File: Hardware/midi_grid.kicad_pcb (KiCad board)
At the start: 2 copper layers, 275 x 200 mm, 329 parts, among them J1 USB_OTG, J2 3.5mm jack, J3 3.5mm jack, J4 Conn_01x04_Male, M1 Mounting_hole, M2 Mounting_hole, M3 Mounting_hole, Q1 BSS83P, Q10 BSS83P, Q11 BSS83P, Q12 BSS83P, Q13 BSS83P, Q14 BSS83P, Q15 BSS83P, Q16 BSS83P, Q17 BSS83P, Q18 BSS83P, Q19 BSS83P, Q2 BSS83P, Q20 BSS83P, Q21 NX7002AK, Q22 NX7002AK, Q23 NX7002AK, Q24 NX7002AK, Q25 NX7002AK, Q26 NX7002AK, Q27 NX7002AK, Q28 NX7002AK, Q29 NX7002AK, Q3 BSS83P, Q30 NX7002AK, Q31 NX7002AK, Q32 NX7002AK, Q33 NX7002AK, Q34 NX7002AK, Q4 BSS83P, Q5 BSS83P, Q6 BSS83P, Q7 BSS83P, Q8 BSS83P, Q9 BSS83P, SW1 Button_matrix_4x4, SW10 SW_Push, SW11 SW_Push, SW12 SW_Push, SW13 SW_Push, SW14 SW_Push, SW15 SW_Push, SW16 SW_Push, SW17 SW_Push, SW18 SW_Push, SW19 SW_Push, SW2 Button_matrix_4x4, SW20 SW_Push, SW21 SW_Push, SW22 SW_Push, SW23 SW_Push, SW24 SW_Push, SW25 EC12E24204A9, SW26 EC12E24204A9, SW3 Button_matrix_4x4, SW4 Button_matrix_4x4, SW5 SW_Push, SW6 SW_Push, SW7 SW_Push, SW8 SW_Push, SW9 SW_Push, U1 STM32F411RCT6, U2 74HC138, U3 74HC138, U4 74HC138, U5 USBUF, U6 LTV-357T, U7 LD1117STR, Y1 8MHz

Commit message: added BOM, changed names of some components in the schematic
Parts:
- Q1, Q10, Q11, Q12, Q13, Q14, Q15, Q16, Q17, Q18, Q19, Q2, Q20, Q3, Q4, Q5, Q6, Q7, Q8, Q9: value BSS83P -> BSH205G2
- R21, R22, R23, R24: value 10K -> 1K
- R25, R26, R27, R28, R33, R34, R35, R36, R41, R42, R43, R44: value 100 -> 100R
- R57, R58, R60, R61, R62: value 220 -> 220R
- U2, U3, U4: value 74HC138 -> SN74HC138PW
- U5: value USBUF -> USBUF02W6
- U6: value LTV-357T -> VO617A

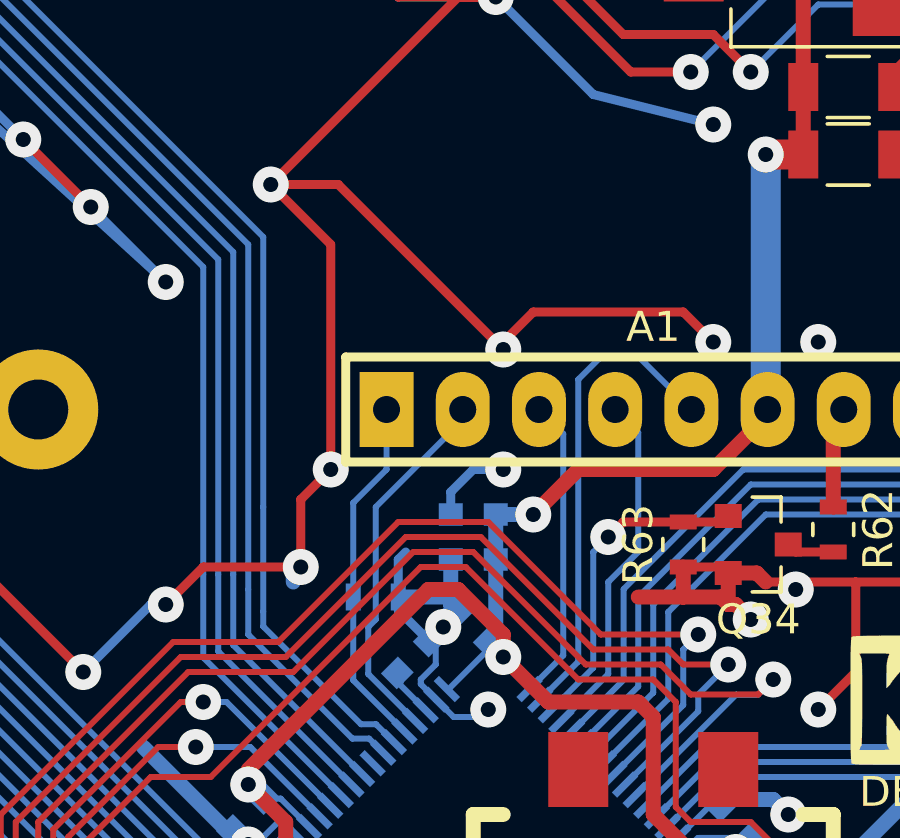
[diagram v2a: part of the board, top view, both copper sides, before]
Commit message: changed pin of LCD CS, so hardware chip select could be used
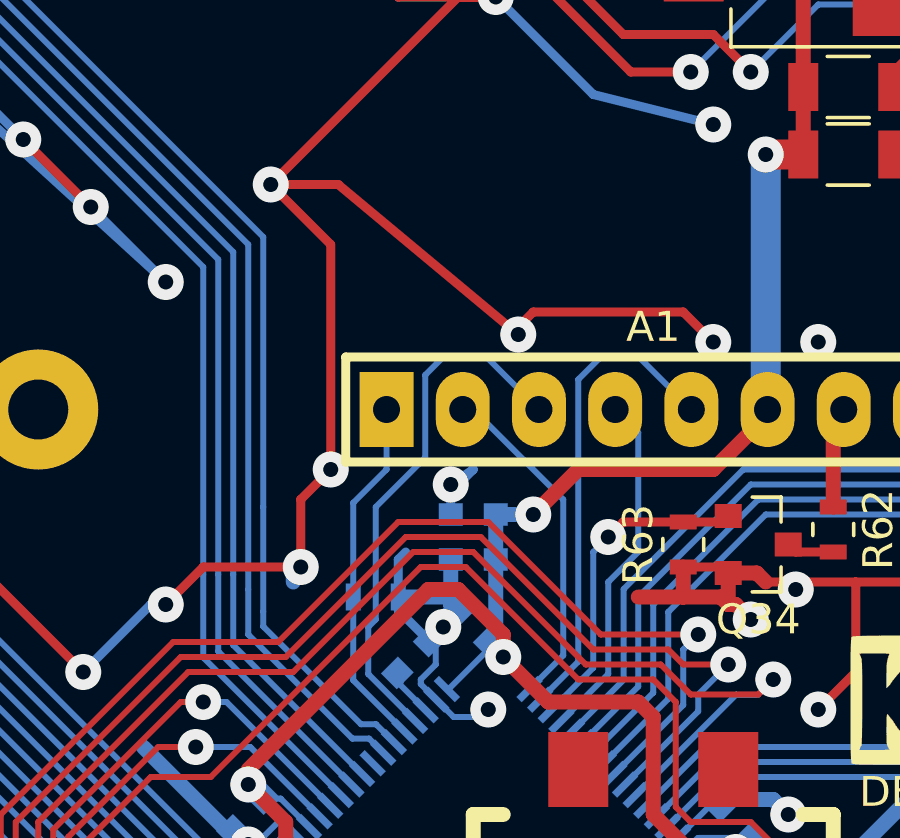
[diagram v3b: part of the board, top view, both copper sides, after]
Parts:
- U2, U3, U4: value SN74HC138PW -> 74HC138
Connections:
- U1 pad 29: /digital_io/LCD_CS -> /digital_io/LCD_DC
- U1 pad 33: /digital_io/LCD_DC -> /digital_io/LCD_CS
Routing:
- net /digital_io/LCD_DC: track 10.1 -> 17.7 mm
- net /digital_io/LCD_CS: track 12.3 -> 11.4 mm
- net GND: track 3946.7 -> 3945.9 mm
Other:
- board text added: "Designed by Gediminas Žukaitis Version 1.1 github.com/zukaitis/midi-grid Date of revision: 2018-01-27"
- board text removed: "Designed by Gediminas Žukaitis Version 1.0 github.com/zukaitis/midi-grid Date of revision: 2018-01-20"
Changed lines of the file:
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@@
     (thickness 1.6)
     (drawings 17)
-    (tracks 4692)
+    (tracks 4697)
     (zones 0)
     (modules 329)
@@
   )
   (setup
-    (last_trace_width 0.5)
+    (last_trace_width 0.2)
     (user_trace_width 0.2)
     (user_trace_width 0.3)
@@
       (effects (font (size 1 1) (thickness 0.15)) (justify mirror))
     )
-    (fp_text value SN74HC138PW (at 0 -3.55) (layer B.Fab)
+    (fp_text value 74HC138 (at 0 -3.55) (layer B.Fab)
       (effects (font (size 1 1) (thickness 0.15)) (justify mirror))
     )
@@
       (effects (font (size 1 1) (thickness 0.15)) (justify mirror))
     )
-    (fp_text value SN74HC138PW (at 0 -3.55 180) (layer B.Fab)
+    (fp_text value 74HC138 (at 0 -3.55 180) (layer B.Fab)
       (effects (font (size 1 1) (thickness 0.15)) (justify mirror))
     )
@@
       (effects (font (size 1 1) (thickness 0.15)) (justify mirror))
     )
-    (fp_text value SN74HC138PW (at 0 -3.55 180) (layer B.Fab)
+    (fp_text value 74HC138 (at 0 -3.55 180) (layer B.Fab)
       (effects (font (size 1 1) (thickness 0.15)) (justify mirror))
     )
@@
       (net 143 /digital_io/LCD_RESET))
     (pad 29 smd rect (at 2.25 -5.7 315) (size 1 0.25) (layers B.Cu B.Paste B.Mask)
-      (net 140 /digital_io/LCD_CS))
+      (net 166 /digital_io/LCD_DC))
     (pad 30 smd rect (at 2.75 -5.7 315) (size 1 0.25) (layers B.Cu B.Paste B.Mask)
       (net 165 /mcu/VCAP))
@@
       (net 2 +3V3))
     (pad 33 smd rect (at 5.7 -3.75 45) (size 1 0.25) (layers B.Cu B.Paste B.Mask)
-      (net 166 /digital_io/LCD_DC))
+      (net 140 /digital_io/LCD_CS))
     (pad 34 smd rect (at 5.7 -3.25 45) (size 1 0.25) (layers B.Cu B.Paste B.Mask)
       (net 141 /digital_io/LCD_SCLK))
@@
     (effects (font (size 1 1) (thickness 0.2)))
   )
-  (gr_text "Designed by Gediminas Žukaitis\nVersion 1.0\ngithub.com/zukaitis/midi-grid\nDate of revision: 2018-01-20" (at 225.5 214.25) (layer B.SilkS)
+  (gr_text "Designed by Gediminas Žukaitis\nVersion 1.1\ngithub.com/zukaitis/midi-grid\nDate of revision: 2018-01-27" (at 225.5 214.25) (layer B.SilkS)
     (effects (font (size 2 2) (thickness 0.4)) (justify left mirror))
   )
@@
   (via (at 268 117.75) (size 1.2) (drill 0.5) (layers F.Cu B.Cu) (net 1))
   (segment (start 268.45 117.3) (end 268 117.75) (width 0.3) (layer B.Cu) (net 1))
-  (segment (start 310.5 78.5) (end 310.5 78.25) (width 0.3) (layer F.Cu) (net 1))
+  (segment (start 311 78) (end 311 77.75) (width 0.3) (layer F.Cu) (net 1))
   (via (at 317.5 78.25) (size 1.2) (drill 0.5) (layers F.Cu B.Cu) (net 1))
   (segment (start 317.5 78) (end 317.5 78.25) (width 0.3) (layer B.Cu) (net 1))
-  (segment (start 305 73) (end 310.5 78.5) (width 0.3) (layer F.Cu) (net 1))
+  (segment (start 305 73) (end 311 78) (width 0.3) (layer F.Cu) (net 1))
   (via (at 302.75 73) (size 1.2) (drill 0.5) (layers F.Cu B.Cu) (net 1))
-  (via (at 310.5 78.5) (size 1.2) (drill 0.5) (layers F.Cu B.Cu) (net 1))
+  (via (at 311 78) (size 1.2) (drill 0.5) (layers F.Cu B.Cu) (net 1))
   (segment (start 305 73) (end 302.75 73) (width 0.3) (layer F.Cu) (net 1))
   (segment (start 316.5 77.25) (end 317.5 78.25) (width 0.3) (layer F.Cu) (net 1))
   (segment (start 311.5 77.25) (end 316.5 77.25) (width 0.3) (layer F.Cu) (net 1))
-  (segment (start 310.5 78.25) (end 311.5 77.25) (width 0.3) (layer F.Cu) (net 1))
+  (segment (start 311 77.75) (end 311.5 77.25) (width 0.3) (layer F.Cu) (net 1))
   (segment (start 303.75 85.75) (end 303.75 83.5) (width 0.3) (layer F.Cu) (net 1))
   (segment (start 303.5 86.25) (end 303.5 86) (width 0.5) (layer B.Cu) (net 1))
@@
   (segment (start 313.25 57.2) (end 313.45 57) (width 0.3) (layer F.Cu) (net 1))
   (segment (start 308.75 84) (end 308.75 83.25) (width 0.3) (layer B.Cu) (net 1))
-  (via (at 310.5 82.5) (size 1.2) (drill 0.5) (layers F.Cu B.Cu) (net 1))
-  (segment (start 309.5 82.5) (end 310.5 82.5) (width 0.3) (layer B.Cu) (net 1))
+  (via (at 308.75 83) (size 1.2) (drill 0.5) (layers F.Cu B.Cu) (net 1))
+  (segment (start 309.5 82.5) (end 308.75 83) (width 0.3) (layer B.Cu) (net 1))
   (segment (start 308.75 83.25) (end 309.5 82.5) (width 0.3) (layer B.Cu) (net 1))
   (segment (start 326.25 135.5) (end 326.25 136.8) (width 0.3) (layer B.Cu) (net 1))
@@
   (segment (start 330 130.25) (end 332 132.25) (width 0.2) (layer B.Cu) (net 139))
   (segment (start 332.25 133.5) (end 332 133.25) (width 0.2) (layer B.Cu) (net 139))
-  (segment (start 306.25 87.5) (end 306.25 83.75) (width 0.2) (layer B.Cu) (net 140))
-  (segment (start 306.25 83.75) (end 309.15 80.85) (width 0.2) (layer B.Cu) (net 140))
-  (segment (start 309.15 80.85) (end 309.15 80.5) (width 0.2) (layer B.Cu) (net 140))
-  (segment (start 307.560482 90.878501) (end 306 89.318019) (width 0.2) (layer B.Cu) (net 140))
-  (segment (start 306 87.75) (end 306.25 87.5) (width 0.2) (layer B.Cu) (net 140))
-  (segment (start 306 89.318019) (end 306 87.75) (width 0.2) (layer B.Cu) (net 140))
+  (segment (start 309.15 80.5) (end 309.5 80.5) (width 0.2) (layer B.Cu) (net 140) (status C00000))
+  (segment (start 309.5 80.5) (end 312.5 83.5) (width 0.2) (layer B.Cu) (net 140) (status 400000))
+  (segment (start 311.378858 89.817841) (end 312.5 88.696699) (width 0.2) (layer B.Cu) (net 140))
+  (segment (start 312.5 88.696699) (end 312.5 83.5) (width 0.2) (layer B.Cu) (net 140))
   (segment (start 311.732412 90.171394) (end 313 88.903806) (width 0.2) (layer B.Cu) (net 141))
   (segment (start 315.02 78.75) (end 316.77 80.5) (width 0.2) (layer B.Cu) (net 141))
@@
   (segment (start 306.96967 89.580583) (end 306.96967 89.28033) (width 0.2) (layer B.Cu) (net 165))
   (segment (start 307.092068 89.570621) (end 307.092068 89.217068) (width 0.2) (layer B.Cu) (net 165))
-  (segment (start 311.378858 89.817841) (end 312.5 88.696699) (width 0.2) (layer B.Cu) (net 166))
-  (segment (start 312.5 81.31) (end 311.69 80.5) (width 0.2) (layer B.Cu) (net 166))
-  (segment (start 312.5 88.696699) (end 312.5 81.31) (width 0.2) (layer B.Cu) (net 166))
+  (segment (start 309.5 78.75) (end 309.94 78.75) (width 0.2) (layer B.Cu) (net 166))
+  (segment (start 307.9 82.1) (end 307.9 79.35) (width 0.2) (layer B.Cu) (net 166))
+  (segment (start 307.9 79.35) (end 308.5 78.75) (width 0.2) (layer B.Cu) (net 166))
+  (segment (start 308.5 78.75) (end 309.5 78.75) (width 0.2) (layer B.Cu) (net 166))
+  (segment (start 306.25 87.5) (end 306.25 83.75) (width 0.2) (layer B.Cu) (net 166))
+  (segment (start 307.560482 90.878501) (end 306 89.318019) (width 0.2) (layer B.Cu) (net 166))
+  (segment (start 306 87.75) (end 306.25 87.5) (width 0.2) (layer B.Cu) (net 166))
+  (segment (start 306 89.318019) (end 306 87.75) (width 0.2) (layer B.Cu) (net 166))
+  (segment (start 306.25 83.75) (end 307.9 82.1) (width 0.2) (layer B.Cu) (net 166))
+  (segment (start 309.94 78.75) (end 311.69 80.5) (width 0.2) (layer B.Cu) (net 166) (status 800000))
   (segment (start 269.45 80.5) (end 270 80.5) (width 0.5) (layer B.Cu) (net 167))
   (segment (start 270 80.5) (end 271 81.5) (width 0.5) (layer B.Cu) (net 167))

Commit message: changed LED current limiting resistor values
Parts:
- R25, R26, R27, R28: value 100R -> 137R
- R33, R34, R35, R36: value 100R -> 93.1R
- R41, R42, R43, R44: value 100R -> 90.9R
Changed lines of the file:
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@@
   )
   (setup
-    (last_trace_width 0.2)
+    (last_trace_width 0.5)
     (user_trace_width 0.2)
     (user_trace_width 0.3)
@@
       (effects (font (size 1 1) (thickness 0.15)) (justify mirror))
     )
-    (fp_text value 100R (at 0 -1.95) (layer B.Fab)
+    (fp_text value 90.9R (at 0 -1.95) (layer B.Fab)
       (effects (font (size 1 1) (thickness 0.15)) (justify mirror))
     )
@@
       (effects (font (size 1 1) (thickness 0.15)) (justify mirror))
     )
-    (fp_text value 100R (at 0 -1.95) (layer B.Fab)
+    (fp_text value 90.9R (at 0 -1.95) (layer B.Fab)
       (effects (font (size 1 1) (thickness 0.15)) (justify mirror))
     )
@@
       (effects (font (size 1 1) (thickness 0.15)) (justify mirror))
     )
-    (fp_text value 100R (at 0 -1.95) (layer B.Fab)
+    (fp_text value 90.9R (at 0 -1.95) (layer B.Fab)
       (effects (font (size 1 1) (thickness 0.15)) (justify mirror))
     )
@@
       (effects (font (size 1 1) (thickness 0.15)) (justify mirror))
     )
-    (fp_text value 100R (at 0 -1.95) (layer B.Fab)
+    (fp_text value 90.9R (at 0 -1.95) (layer B.Fab)
       (effects (font (size 1 1) (thickness 0.15)) (justify mirror))
     )
@@
       (effects (font (size 1 1) (thickness 0.15)) (justify mirror))
     )
-    (fp_text value 100R (at 0 -1.95 90) (layer B.Fab)
+    (fp_text value 93.1R (at 0 -1.95 90) (layer B.Fab)
       (effects (font (size 1 1) (thickness 0.15)) (justify mirror))
     )
@@
       (effects (font (size 1 1) (thickness 0.15)) (justify mirror))
     )
-    (fp_text value 100R (at 0 -1.95 90) (layer B.Fab)
+    (fp_text value 93.1R (at 0 -1.95 90) (layer B.Fab)
       (effects (font (size 1 1) (thickness 0.15)) (justify mirror))
     )
@@
       (effects (font (size 1 1) (thickness 0.15)) (justify mirror))
     )
-    (fp_text value 100R (at 0 -1.95 90) (layer B.Fab)
+    (fp_text value 93.1R (at 0 -1.95 90) (layer B.Fab)
       (effects (font (size 1 1) (thickness 0.15)) (justify mirror))
     )
@@
       (effects (font (size 1 1) (thickness 0.15)) (justify mirror))
     )
-    (fp_text value 100R (at 0 -1.95 90) (layer B.Fab)
+    (fp_text value 93.1R (at 0 -1.95 90) (layer B.Fab)
       (effects (font (size 1 1) (thickness 0.15)) (justify mirror))
     )
@@
       (effects (font (size 1 1) (thickness 0.15)) (justify mirror))
     )
-    (fp_text value 100R (at 0 -1.95) (layer B.Fab)
+    (fp_text value 137R (at 0 -1.95) (layer B.Fab)
       (effects (font (size 1 1) (thickness 0.15)) (justify mirror))
     )
@@
       (effects (font (size 1 1) (thickness 0.15)) (justify mirror))
     )
-    (fp_text value 100R (at 0 -1.95) (layer B.Fab)
+    (fp_text value 137R (at 0 -1.95) (layer B.Fab)
       (effects (font (size 1 1) (thickness 0.15)) (justify mirror))
     )
@@
       (effects (font (size 1 1) (thickness 0.15)) (justify mirror))
     )
-    (fp_text value 100R (at 0 -1.95) (layer B.Fab)
+    (fp_text value 137R (at 0 -1.95) (layer B.Fab)
       (effects (font (size 1 1) (thickness 0.15)) (justify mirror))
     )
@@
       (effects (font (size 1 1) (thickness 0.15)) (justify mirror))
     )
-    (fp_text value 100R (at 0 -1.95) (layer B.Fab)
+    (fp_text value 137R (at 0 -1.95) (layer B.Fab)
       (effects (font (size 1 1) (thickness 0.15)) (justify mirror))
     )
@@
   (segment (start 330 130.25) (end 332 132.25) (width 0.2) (layer B.Cu) (net 139))
   (segment (start 332.25 133.5) (end 332 133.25) (width 0.2) (layer B.Cu) (net 139))
-  (segment (start 309.15 80.5) (end 309.5 80.5) (width 0.2) (layer B.Cu) (net 140) (status C00000))
-  (segment (start 309.5 80.5) (end 312.5 83.5) (width 0.2) (layer B.Cu) (net 140) (status 400000))
+  (segment (start 309.15 80.5) (end 309.5 80.5) (width 0.2) (layer B.Cu) (net 140))
+  (segment (start 309.5 80.5) (end 312.5 83.5) (width 0.2) (layer B.Cu) (net 140))
   (segment (start 311.378858 89.817841) (end 312.5 88.696699) (width 0.2) (layer B.Cu) (net 140))
   (segment (start 312.5 88.696699) (end 312.5 83.5) (width 0.2) (layer B.Cu) (net 140))
@@
   (segment (start 306 89.318019) (end 306 87.75) (width 0.2) (layer B.Cu) (net 166))
   (segment (start 306.25 83.75) (end 307.9 82.1) (width 0.2) (layer B.Cu) (net 166))
-  (segment (start 309.94 78.75) (end 311.69 80.5) (width 0.2) (layer B.Cu) (net 166) (status 800000))
+  (segment (start 309.94 78.75) (end 311.69 80.5) (width 0.2) (layer B.Cu) (net 166))
   (segment (start 269.45 80.5) (end 270 80.5) (width 0.5) (layer B.Cu) (net 167))
   (segment (start 270 80.5) (end 271 81.5) (width 0.5) (layer B.Cu) (net 167))

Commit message: changed resistor values, added drum layout output
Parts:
- R25, R26, R27, R28: value 137R -> 249R
- R33, R34, R35, R36: value 93.1R -> 294R
- R41, R42, R43, R44: value 90.9R -> 51R
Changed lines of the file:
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@@
       (effects (font (size 1 1) (thickness 0.15)) (justify mirror))
     )
-    (fp_text value 90.9R (at 0 -1.95) (layer B.Fab)
+    (fp_text value 51R (at 0 -1.95) (layer B.Fab)
       (effects (font (size 1 1) (thickness 0.15)) (justify mirror))
     )
@@
       (effects (font (size 1 1) (thickness 0.15)) (justify mirror))
     )
-    (fp_text value 90.9R (at 0 -1.95) (layer B.Fab)
+    (fp_text value 51R (at 0 -1.95) (layer B.Fab)
       (effects (font (size 1 1) (thickness 0.15)) (justify mirror))
     )
@@
       (effects (font (size 1 1) (thickness 0.15)) (justify mirror))
     )
-    (fp_text value 90.9R (at 0 -1.95) (layer B.Fab)
+    (fp_text value 51R (at 0 -1.95) (layer B.Fab)
       (effects (font (size 1 1) (thickness 0.15)) (justify mirror))
     )
@@
       (effects (font (size 1 1) (thickness 0.15)) (justify mirror))
     )
-    (fp_text value 90.9R (at 0 -1.95) (layer B.Fab)
+    (fp_text value 51R (at 0 -1.95) (layer B.Fab)
       (effects (font (size 1 1) (thickness 0.15)) (justify mirror))
     )
@@
       (effects (font (size 1 1) (thickness 0.15)) (justify mirror))
     )
-    (fp_text value 93.1R (at 0 -1.95 90) (layer B.Fab)
+    (fp_text value 294R (at 0 -1.95 90) (layer B.Fab)
       (effects (font (size 1 1) (thickness 0.15)) (justify mirror))
     )
@@
       (effects (font (size 1 1) (thickness 0.15)) (justify mirror))
     )
-    (fp_text value 93.1R (at 0 -1.95 90) (layer B.Fab)
+    (fp_text value 294R (at 0 -1.95 90) (layer B.Fab)
       (effects (font (size 1 1) (thickness 0.15)) (justify mirror))
     )
@@
       (effects (font (size 1 1) (thickness 0.15)) (justify mirror))
     )
-    (fp_text value 93.1R (at 0 -1.95 90) (layer B.Fab)
+    (fp_text value 294R (at 0 -1.95 90) (layer B.Fab)
       (effects (font (size 1 1) (thickness 0.15)) (justify mirror))
     )
@@
       (effects (font (size 1 1) (thickness 0.15)) (justify mirror))
     )
-    (fp_text value 93.1R (at 0 -1.95 90) (layer B.Fab)
+    (fp_text value 294R (at 0 -1.95 90) (layer B.Fab)
       (effects (font (size 1 1) (thickness 0.15)) (justify mirror))
     )
@@
       (effects (font (size 1 1) (thickness 0.15)) (justify mirror))
     )
-    (fp_text value 137R (at 0 -1.95) (layer B.Fab)
+    (fp_text value 249R (at 0 -1.95) (layer B.Fab)
       (effects (font (size 1 1) (thickness 0.15)) (justify mirror))
     )
@@
       (effects (font (size 1 1) (thickness 0.15)) (justify mirror))
     )
-    (fp_text value 137R (at 0 -1.95) (layer B.Fab)
+    (fp_text value 249R (at 0 -1.95) (layer B.Fab)
       (effects (font (size 1 1) (thickness 0.15)) (justify mirror))
     )
@@
       (effects (font (size 1 1) (thickness 0.15)) (justify mirror))
     )
-    (fp_text value 137R (at 0 -1.95) (layer B.Fab)
+    (fp_text value 249R (at 0 -1.95) (layer B.Fab)
       (effects (font (size 1 1) (thickness 0.15)) (justify mirror))
     )
@@
       (effects (font (size 1 1) (thickness 0.15)) (justify mirror))
     )
-    (fp_text value 137R (at 0 -1.95) (layer B.Fab)
-      (effects (font (size 1 1) (thickness 0.15)) (justify mirror))
-    )
+    (fp_text value 249R (at 0 -1.95) (layer B.Fab)
+      (effects (font (size 1 1) (thickness 0.15)) (justify mirror))
+    )
